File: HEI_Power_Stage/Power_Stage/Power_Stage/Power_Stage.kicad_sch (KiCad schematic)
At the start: 38 parts, among them IC4 AMC1311DWVR, IC9 ACS730KLCTR-65ABT, J1 Screw_Terminal_01x01, J2 Screw_Terminal_01x01, J3 Screw_Terminal_01x01, J4 Screw_Terminal_01x01, J5 Screw_Terminal_01x01, J8 Conn_02x07_Odd_Even, J9 Conn_02x07_Odd_Even

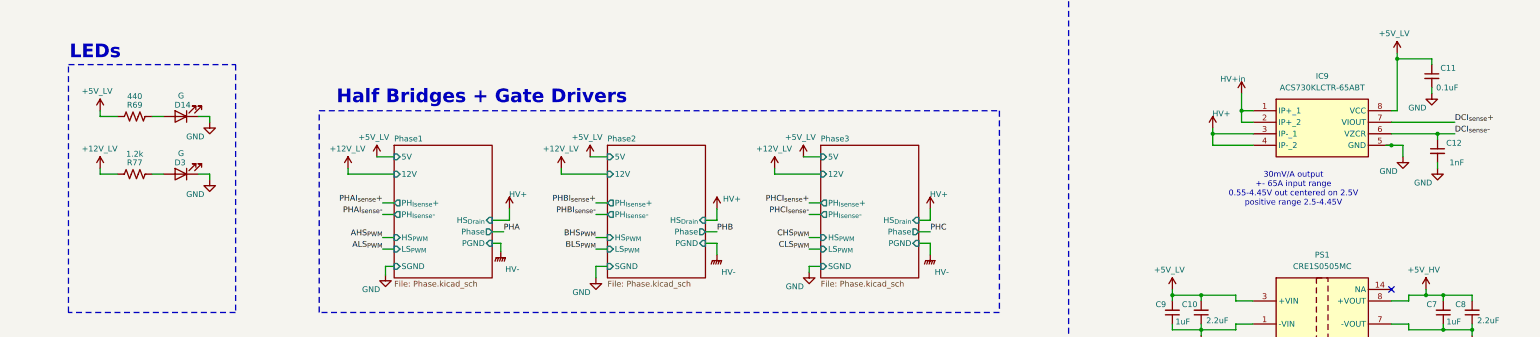
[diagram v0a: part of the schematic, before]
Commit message: done
silkscreen done and bom done in digikey
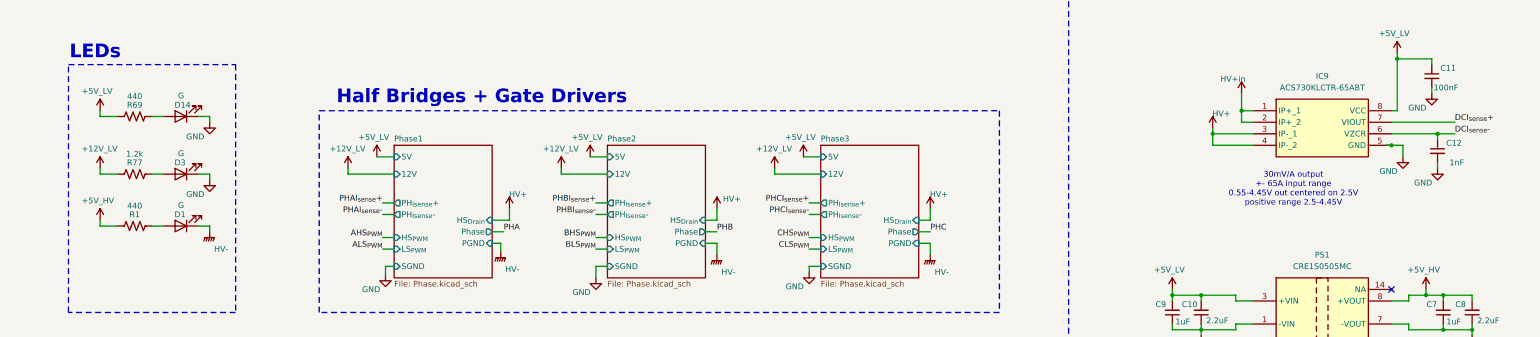
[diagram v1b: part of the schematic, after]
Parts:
- added D1: G, LED_SMD:LED_0603_1608Metric_Pad1.05x0.95mm_HandSolder, symbol Device:LED
- added R1: 440, Resistor_SMD:R_0603_1608Metric_Pad0.98x0.95mm_HandSolder, symbol Device:R_US
- C11: value 0.1uF -> 100nF
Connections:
- net +5V_HV: now also R1.2
- net HV-: now also D1.1 (K)
- new net: D1.2 (A), R1.1

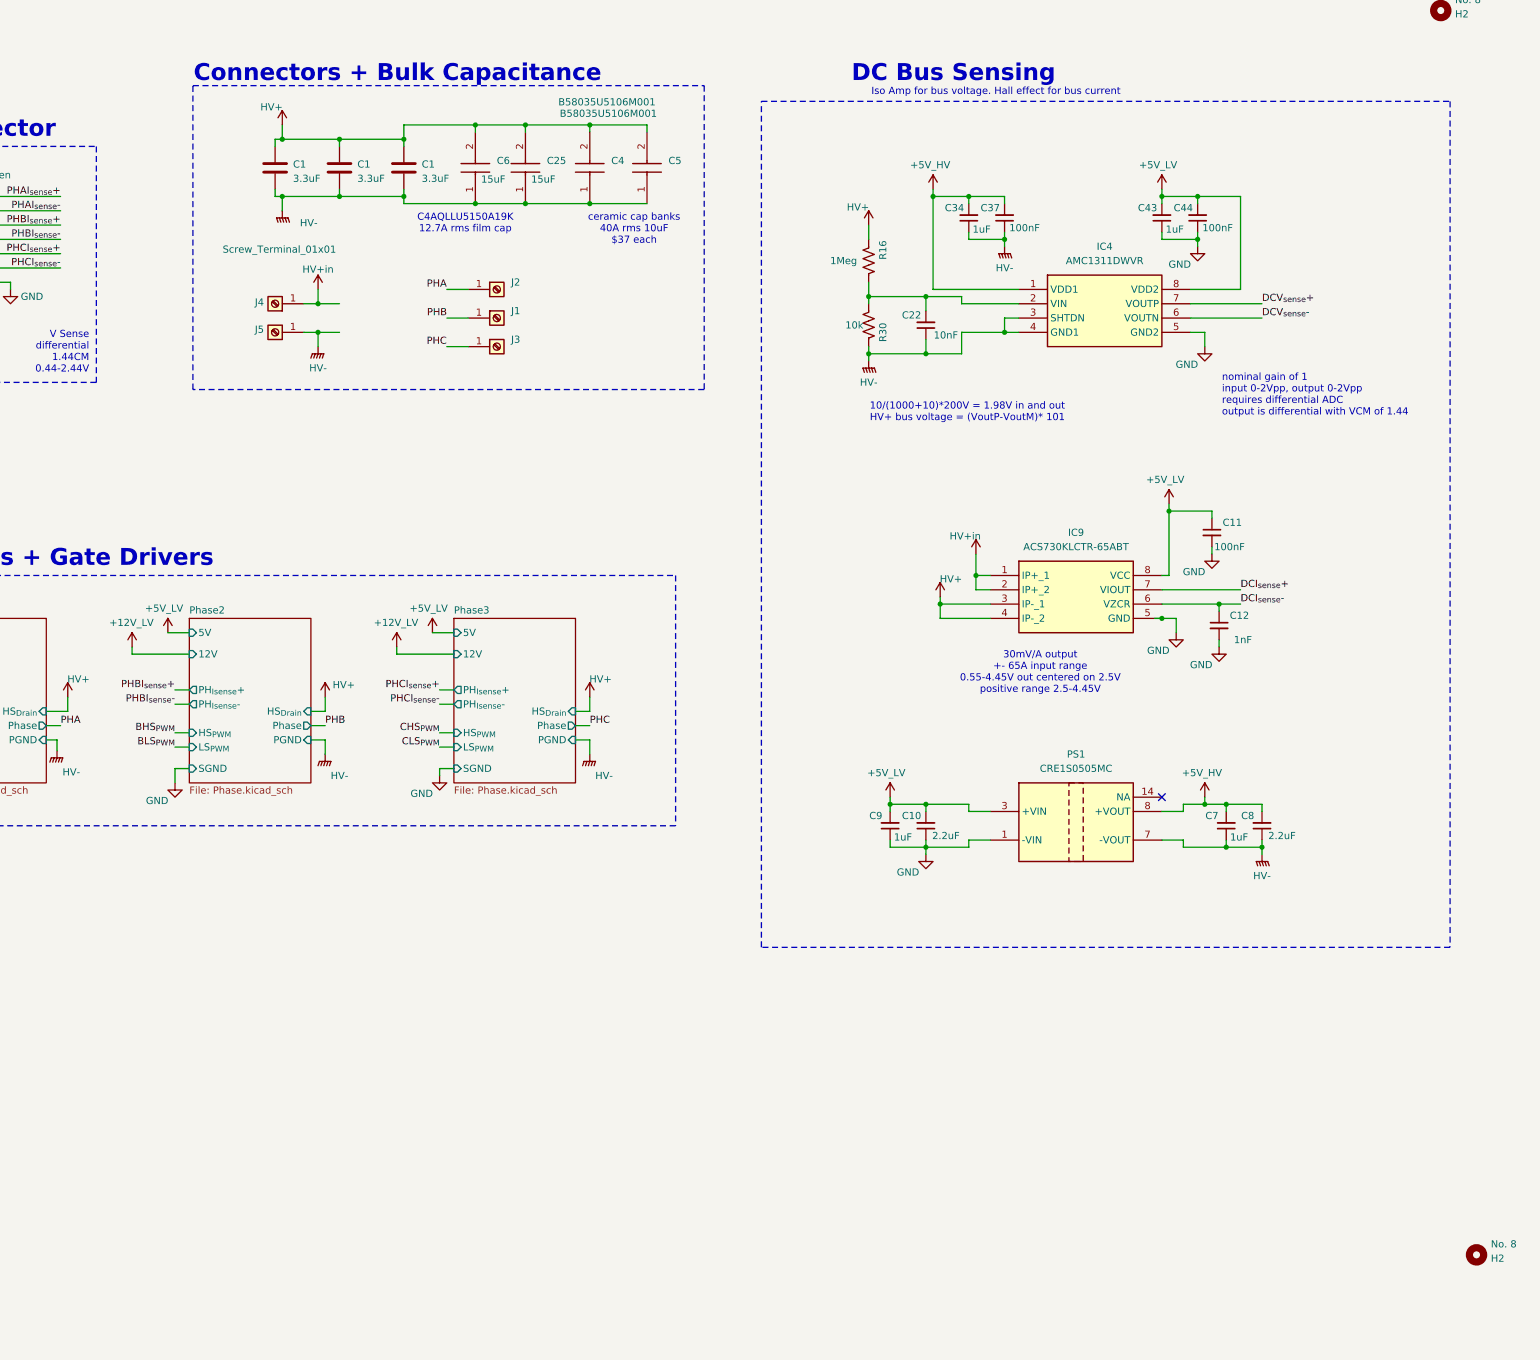
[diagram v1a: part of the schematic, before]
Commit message: some changes
isolated amplifier now self powered so removed old amp and iso power supply
gate return paths now on layer two
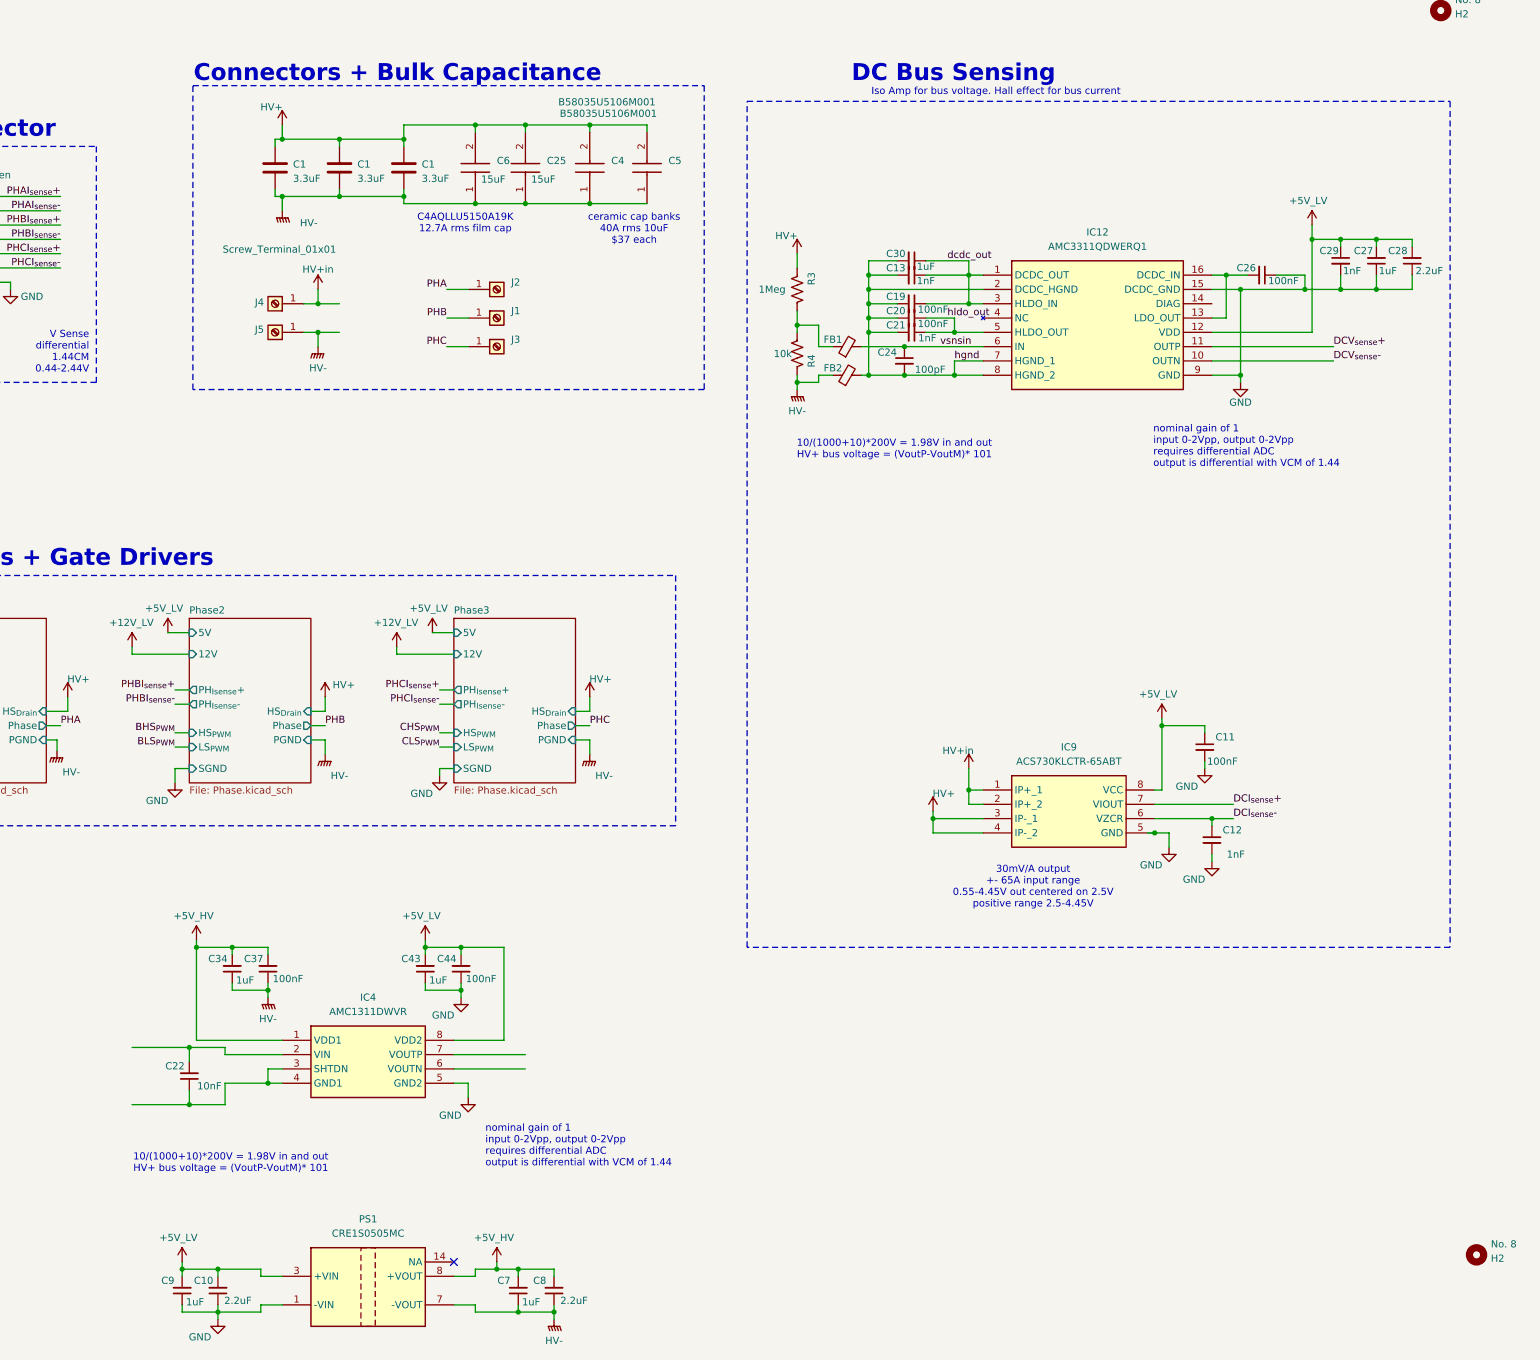
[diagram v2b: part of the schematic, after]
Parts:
- removed R16: 1Meg, Resistor_SMD:R_1206_3216Metric, symbol Device:R_US
- removed R30: 10k, Resistor_SMD:R_1206_3216Metric, symbol Device:R_US
- added C13, C21, C29: 1nF, Capacitor_SMD:C_0603_1608Metric_Pad1.08x0.95mm_HandSolder, symbol Device:C_Small
- added C19, C20, C26: 100nF, Capacitor_SMD:C_0603_1608Metric_Pad1.08x0.95mm_HandSolder, symbol Device:C_Small
- added C24: 100pF, Capacitor_SMD:C_0603_1608Metric_Pad1.08x0.95mm_HandSolder, symbol Device:C_Small
- added C27, C30: 1uF, Capacitor_SMD:C_0603_1608Metric_Pad1.08x0.95mm_HandSolder, symbol Device:C_Small
- added C28: 2.2uF, Capacitor_SMD:C_0603_1608Metric_Pad1.08x0.95mm_HandSolder, symbol Device:C_Small
- added FB1, FB2: ~, Resistor_SMD:R_0603_1608Metric_Pad0.98x0.95mm_HandSolder, symbol Device:FerriteBead_Small
- added IC12: AMC3311QDWERQ1, AMC3311_KiCad:SOIC127P1030X265-16N, symbol AMC3311QDWERQ1:AMC3311QDWERQ1
- added R3: 1Meg, Resistor_SMD:R_1206_3216Metric, symbol Device:R_US
- added R4: 10k, Resistor_SMD:R_1206_3216Metric, symbol Device:R_US
- H2: footprint MountingHole:MountingHole_2.1mm -> MountingHole:MountingHole_3.2mm_M3
- PS1: footprint CRE1S0505MC -> CRE1S0505MC_KiCad:CRE1S0505MC
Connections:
- net +5V_LV: now also C27.2, C28.2, C29.1, IC12.12 (VDD)
- net DCV_{sense}+: now also IC12.11 (OUTP); no longer IC4.7 (VOUTP)
- net DCV_{sense}-: now also IC12.10 (OUTN); no longer IC4.6 (VOUTN)
- net GND: now also C26.1, C27.1, C28.1, C29.2, IC12.15 (DCDC_GND), IC12.9 (GND)
- net HV+: now also R3.2
- net HV-: now also FB2.1, R4.1; no longer C22.1, IC4.3 (SHTDN), IC4.4 (GND1)
- new net: FB1.1, R3.1, R4.2
- new net: C26.2, IC12.13 (LDO_OUT), IC12.16 (DCDC_IN)
- new net: C22.1, IC4.3 (SHTDN), IC4.4 (GND1)
- new net dcdc_out: C13.1, C19.1, C30.1, IC12.1 (DCDC_OUT), IC12.3 (HLDO_IN)
- new net hgnd: C13.2, C19.2, C20.2, C21.2, C24.2, C30.2, FB2.2, IC12.2 (DCDC_HGND), IC12.7 (HGND_1), IC12.8 (HGND_2)
- new net hldo_out: C20.1, C21.1, IC12.5 (HLDO_OUT)
- new net vsnsin: C24.1, FB1.2, IC12.6 (IN)
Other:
- moved on the sheet: C10, C11, C12, C22, C34, C37, C43, C44, C7, C8, C9, IC4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

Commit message: removed extra parts
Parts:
- removed C10, C8: 2.2uF, Capacitor_SMD:C_0603_1608Metric_Pad1.08x0.95mm_HandSolder, symbol Device:C_Small
- removed C22: 10nF, Capacitor_SMD:C_0603_1608Metric_Pad1.08x0.95mm_HandSolder, symbol Device:C_Small
- removed C34, C43, C7, C9: 1uF, Capacitor_SMD:C_0603_1608Metric_Pad1.08x0.95mm_HandSolder, symbol Device:C_Small
- removed C37, C44: 100nF, Capacitor_SMD:C_0603_1608Metric_Pad1.08x0.95mm_HandSolder, symbol Device:C_Small
- removed IC4: AMC1311DWVR, AMC1311_KiCad:SOIC127P1150X280-8N, symbol AMC1311DWVR:AMC1311DWVR
- removed PS1: CRE1S0505MC, CRE1S0505MC_KiCad:CRE1S0505MC, symbol CRE1S0505MC:CRE1S0505MC
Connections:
- no-connect marks 1 -> 9
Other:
- moved on the sheet: C11, C12, IC9

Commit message: final changes and bom with digikey and mouser PN
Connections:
- net GND: now also J8.1 (Pin_1), J8.11 (Pin_11), J8.3 (Pin_3), J8.5 (Pin_5), J8.7 (Pin_7), J8.9 (Pin_9), J9.11 (Pin_11), J9.9 (Pin_9)
- no-connect marks 9 -> 1
